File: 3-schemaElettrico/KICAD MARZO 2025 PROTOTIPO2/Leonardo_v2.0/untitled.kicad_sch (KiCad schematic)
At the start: 0 parts

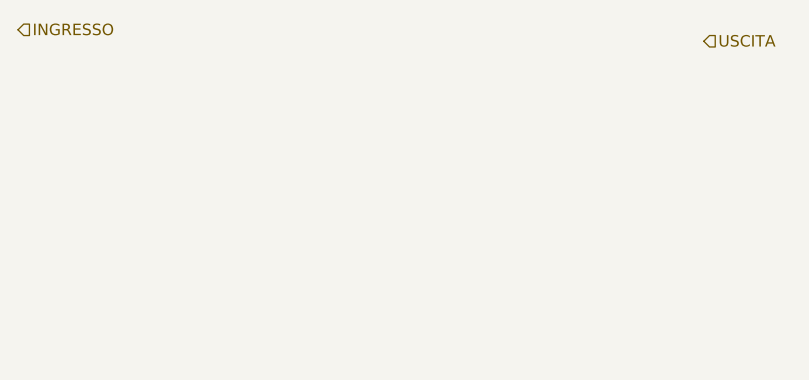
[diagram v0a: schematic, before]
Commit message: done 74hc238
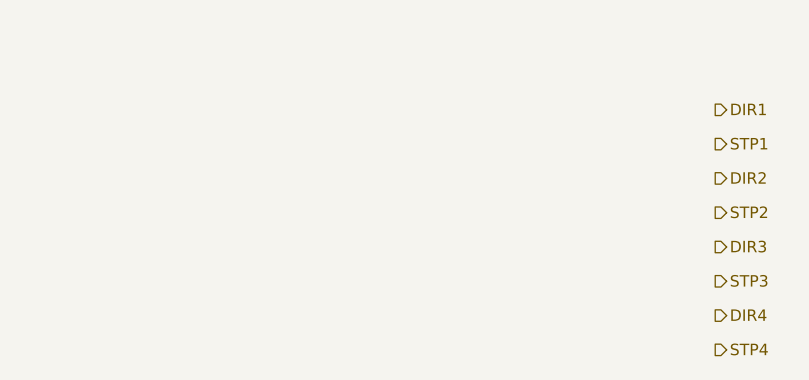
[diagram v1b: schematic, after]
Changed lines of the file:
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@@
 	(generator_version "9.0")
 	(paper "A4")
-	(hierarchical_label "INGRESSO"
-		(shape input)
-		(at 83.82 68.58 0)
+	(hierarchical_label "DIR2"
+		(shape output)
+		(at 161.29 85.09 0)
 		(effects
 			(font
@@
 		)
 	)
-	(hierarchical_label "USCITA"
-		(shape input)
-		(at 160.02 69.85 0)
+	(hierarchical_label "STP4"
+		(shape output)
+		(at 161.29 104.14 0)
 		(effects
 			(font
+				(size 1.27 1.27)
+			)
+			(justify left)
+		)
+	)
+	(hierarchical_label "STP2"
+		(shape output)
+		(at 161.29 88.9 0)
+		(effects
+			(font
+				(size 1.27 1.27)
+			)
+			(justify left)
+		)
+	)
+	(hierarchical_label "STP1"
+		(shape output)
+		(at 161.29 81.28 0)
+		(effects
+			(font
+				(size 1.27 1.27)
+			)
+			(justify left)
+		)
+	)
+	(hierarchical_label "DIR1"
+		(shape output)
+		(at 161.29 77.47 0)
+		(effects
+			(font
+				(size 1.27 1.27)
+			)
+			(justify left)
+		)
+	)
+	(hierarchical_label "DIR3"
+		(shape output)
+		(at 161.29 92.71 0)
+		(effects
+			(font
+				(size 1.27 1.27)
+			)
+			(justify left)
+		)
+	)
+	(hierarchical_label "DIR4"
+		(shape output)
+		(at 161.29 100.33 0)
+		(effects
+			(font
+				(size 1.27 1.27)
+			)
+			(justify left)
+		)
+	)
+	(hierarchical_label "STP3"
+		(shape output)
+		(at 161.29 96.52 0)
+		(effects
+			(font
